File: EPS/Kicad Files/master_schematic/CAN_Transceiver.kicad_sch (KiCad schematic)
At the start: 5 parts, among them U3 ATA6560-GAQW-VAO

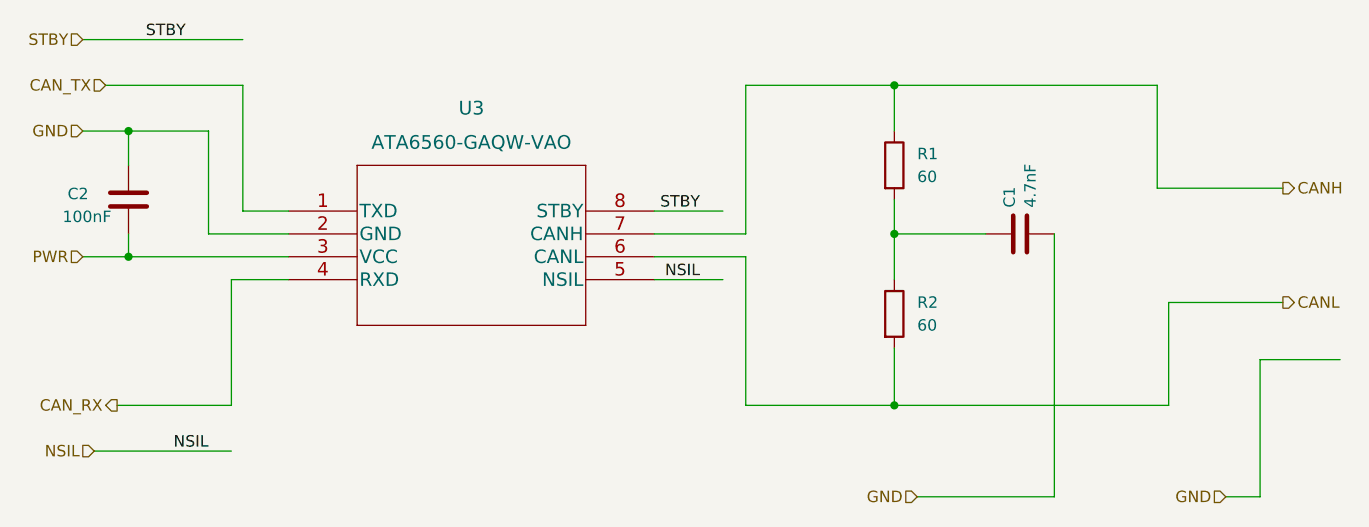
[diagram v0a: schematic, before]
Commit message: updated master schematic
should be nearing final schematic revision. run electrical rules check next
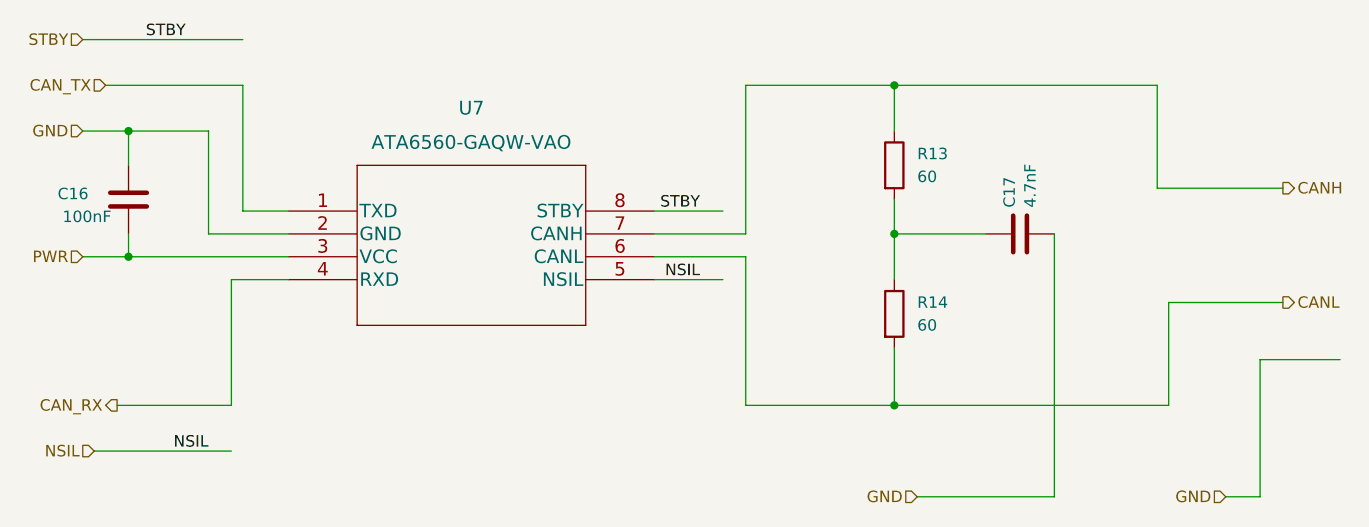
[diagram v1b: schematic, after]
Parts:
- C16: renamed from C2; footprint Capacitor_SMD:C_0603_1608Metric_Pad1.08x0.95mm_HandSolder -> Capacitor_SMD:C_0603_1608Metric
- C17: renamed from C1; footprint Capacitor_SMD:C_0603_1608Metric_Pad1.08x0.95mm_HandSolder -> Capacitor_SMD:C_0603_1608Metric
- R13: renamed from R1; footprint Resistor_SMD:R_0603_1608Metric_Pad0.98x0.95mm_HandSolder -> Resistor_SMD:R_0603_1608Metric
- R14: renamed from R2; footprint Resistor_SMD:R_0603_1608Metric_Pad0.98x0.95mm_HandSolder -> Resistor_SMD:R_0603_1608Metric
- renumbered U3 to U7
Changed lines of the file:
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@@
   (symbol (lib_id "Device:R") (at 173.99 107.95 0) (unit 1)
     (in_bom yes) (on_board yes)
-    (property "Reference" "R2" (id 0) (at 176.53 106.6799 0)
+    (property "Reference" "R14" (id 0) (at 176.53 106.6799 0)
       (effects (font (size 1.27 1.27)) (justify left))
     )
@@
       (effects (font (size 1.27 1.27)) (justify left))
     )
-    (property "Footprint" "Resistor_SMD:R_0603_1608Metric_Pad0.98x0.95mm_HandSolder" (id 2) (at 172.212 107.95 90)
+    (property "Footprint" "Resistor_SMD:R_0603_1608Metric" (id 2) (at 172.212 107.95 90)
       (effects (font (size 1.27 1.27)) hide)
     )
@@
   (symbol (lib_id "Device:C") (at 88.9 95.25 180) (unit 1)
     (in_bom yes) (on_board yes)
-    (property "Reference" "C2" (id 0) (at 84.455 94.615 0)
+    (property "Reference" "C16" (id 0) (at 84.455 94.615 0)
       (effects (font (size 1.27 1.27)) (justify left))
     )
@@
       (effects (font (size 1.27 1.27)) (justify left))
     )
-    (property "Footprint" "Capacitor_SMD:C_0603_1608Metric_Pad1.08x0.95mm_HandSolder" (id 2) (at 87.9348 91.44 0)
+    (property "Footprint" "Capacitor_SMD:C_0603_1608Metric" (id 2) (at 87.9348 91.44 0)
       (effects (font (size 1.27 1.27)) hide)
     )
@@
   (symbol (lib_id "Device:C") (at 187.96 99.06 90) (unit 1)
     (in_bom yes) (on_board yes)
-    (property "Reference" "C1" (id 0) (at 186.7916 96.139 0)
+    (property "Reference" "C17" (id 0) (at 186.7916 96.139 0)
       (effects (font (size 1.27 1.27)) (justify left))
     )
@@
       (effects (font (size 1.27 1.27)) (justify left))
     )
-    (property "Footprint" "Capacitor_SMD:C_0603_1608Metric_Pad1.08x0.95mm_HandSolder" (id 2) (at 191.77 98.0948 0)
+    (property "Footprint" "Capacitor_SMD:C_0603_1608Metric" (id 2) (at 191.77 98.0948 0)
       (effects (font (size 1.27 1.27)) hide)
     )
@@
   (symbol (lib_id "Device:R") (at 173.99 91.44 0) (unit 1)
     (in_bom yes) (on_board yes) (fields_autoplaced)
-    (property "Reference" "R1" (id 0) (at 176.53 90.1699 0)
+    (property "Reference" "R13" (id 0) (at 176.53 90.1699 0)
       (effects (font (size 1.27 1.27)) (justify left))
     )
@@
       (effects (font (size 1.27 1.27)) (justify left))
     )
-    (property "Footprint" "Resistor_SMD:R_0603_1608Metric_Pad0.98x0.95mm_HandSolder" (id 2) (at 172.212 91.44 90)
+    (property "Footprint" "Resistor_SMD:R_0603_1608Metric" (id 2) (at 172.212 91.44 90)
       (effects (font (size 1.27 1.27)) hide)
     )
@@
   (symbol (lib_id "2022-01-28_19-14-47:ATA6560-GAQW-VAO") (at 106.68 96.52 0) (unit 1)
     (in_bom yes) (on_board yes) (fields_autoplaced)
-    (property "Reference" "U3" (id 0) (at 127 85.09 0)
+    (property "Reference" "U7" (id 0) (at 127 85.09 0)
       (effects (font (size 1.524 1.524)))
     )

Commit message: EPS master netlist complete
dropped all parts onto pcb
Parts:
- U7: footprint CAN_footprint:ATA6560-GAQW-VAO -> ata6560:ATA6560-GAQW-VAO
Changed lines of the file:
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@@
       (effects (font (size 1.524 1.524)))
     )
-    (property "Footprint" "CAN_footprint:ATA6560-GAQW-VAO" (id 2) (at 127 90.424 0)
+    (property "Footprint" "ata6560:ATA6560-GAQW-VAO" (id 2) (at 127 90.424 0)
       (effects (font (size 1.524 1.524)) hide)
     )
